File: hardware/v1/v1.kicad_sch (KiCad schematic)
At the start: 70 parts, among them J1 AUDIO IN, J10 Close for battery power, J2 MIDI OUT, J3 MIDI IN, J4 MIDI THRU, J5 OUTPUT R, J6 OUTPUT L - MONO, J7 EXP 2, J8 EXP 1, J9 Batt In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

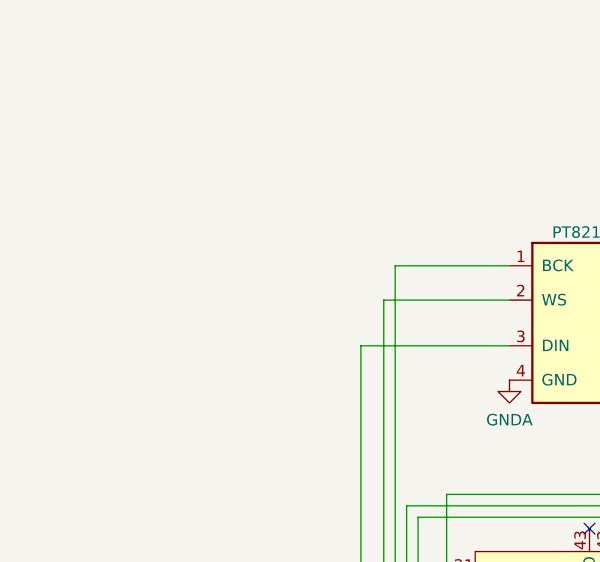
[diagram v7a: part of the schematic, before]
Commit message: Added mounting holes - Cleaned PCB placement
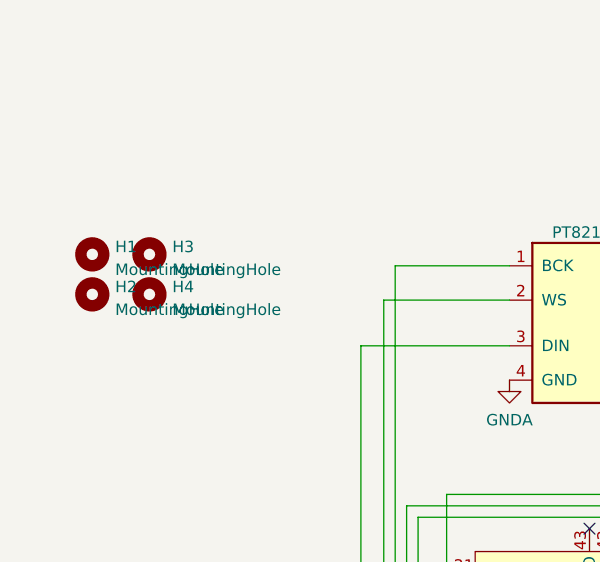
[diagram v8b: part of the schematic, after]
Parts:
- added H1, H2, H3, H4: MountingHole, MountingHole:MountingHole_3.2mm_M3_ISO14580, symbol Mechanical:MountingHole
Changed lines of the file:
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@@
     (pin "8")
+  )
+  (symbol (lib_id "Mechanical:MountingHole") (at 26.035 31.75 0) (unit 1)
+    (in_bom yes) (on_board yes) (fields_autoplaced)
+    (property "Reference" "H1" (id 0) (at 28.575 30.9153 0)
+      (effects (font (size 1.27 1.27)) (justify left))
+    )
+    (property "Value" "MountingHole" (id 1) (at 28.575 33.4522 0)
+      (effects (font (size 1.27 1.27)) (justify left))
+    )
+    (property "Footprint" "MountingHole:MountingHole_3.2mm_M3_ISO14580" (id 2) (at 26.035 31.75 0)
+      (effects (font (size 1.27 1.27)) hide)
+    )
+    (property "Datasheet" "~" (id 3) (at 26.035 31.75 0)
+      (effects (font (size 1.27 1.27)) hide)
+    )
   )
   (symbol (lib_id "power:+3V3") (at 159.385 73.66 90) (unit 1)
@@
     (pin "4")
   )
+  (symbol (lib_id "Mechanical:MountingHole") (at 32.385 31.75 0) (unit 1)
+    (in_bom yes) (on_board yes) (fields_autoplaced)
+    (property "Reference" "H3" (id 0) (at 34.925 30.9153 0)
+      (effects (font (size 1.27 1.27)) (justify left))
+    )
+    (property "Value" "MountingHole" (id 1) (at 34.925 33.4522 0)
+      (effects (font (size 1.27 1.27)) (justify left))
+    )
+    (property "Footprint" "MountingHole:MountingHole_3.2mm_M3_ISO14580" (id 2) (at 32.385 31.75 0)
+      (effects (font (size 1.27 1.27)) hide)
+    )
+    (property "Datasheet" "~" (id 3) (at 32.385 31.75 0)
+      (effects (font (size 1.27 1.27)) hide)
+    )
+  )
   (symbol (lib_id "Device:C_Polarized") (at 455.295 149.225 180) (unit 1)
     (in_bom yes) (on_board yes) (fields_autoplaced)
@@
     (pin "4")
   )
+  (symbol (lib_id "Mechanical:MountingHole") (at 26.035 36.195 0) (unit 1)
+    (in_bom yes) (on_board yes) (fields_autoplaced)
+    (property "Reference" "H2" (id 0) (at 28.575 35.3603 0)
+      (effects (font (size 1.27 1.27)) (justify left))
+    )
+    (property "Value" "MountingHole" (id 1) (at 28.575 37.8972 0)
+      (effects (font (size 1.27 1.27)) (justify left))
+    )
+    (property "Footprint" "MountingHole:MountingHole_3.2mm_M3_ISO14580" (id 2) (at 26.035 36.195 0)
+      (effects (font (size 1.27 1.27)) hide)
+    )
+    (property "Datasheet" "~" (id 3) (at 26.035 36.195 0)
+      (effects (font (size 1.27 1.27)) hide)
+    )
+  )
   (symbol (lib_id "Amplifier_Operational:TL074") (at 408.94 120.015 0) (unit 2)
     (in_bom yes) (on_board yes) (fields_autoplaced)
@@
     (pin "2")
     (pin "3")
+  )
+  (symbol (lib_id "Mechanical:MountingHole") (at 32.385 36.195 0) (unit 1)
+    (in_bom yes) (on_board yes) (fields_autoplaced)
+    (property "Reference" "H4" (id 0) (at 34.925 35.3603 0)
+      (effects (font (size 1.27 1.27)) (justify left))
+    )
+    (property "Value" "MountingHole" (id 1) (at 34.925 37.8972 0)
+      (effects (font (size 1.27 1.27)) (justify left))
+    )
+    (property "Footprint" "MountingHole:MountingHole_3.2mm_M3_ISO14580" (id 2) (at 32.385 36.195 0)
+      (effects (font (size 1.27 1.27)) hide)
+    )
+    (property "Datasheet" "~" (id 3) (at 32.385 36.195 0)
+      (effects (font (size 1.27 1.27)) hide)
+    )
   )
   (symbol (lib_id "power:+3.3V") (at 191.135 137.795 90) (unit 1)
@@
       (reference "D1") (unit 1) (value "1N914") (footprint "Diode_THT:D_DO-34_SOD68_P7.62mm_Horizontal")
     )
+    (path "/1b38fedc-9922-4b9f-a208-ce686a48a281"
+      (reference "H1") (unit 1) (value "MountingHole") (footprint "MountingHole:MountingHole_3.2mm_M3_ISO14580")
+    )
+    (path "/716e12c1-8bb1-4d40-9e17-8109f40cc3b6"
+      (reference "H2") (unit 1) (value "MountingHole") (footprint "MountingHole:MountingHole_3.2mm_M3_ISO14580")
+    )
+    (path "/66c12bc5-3179-47f4-bb5e-65b70f04e9af"
+      (reference "H3") (unit 1) (value "MountingHole") (footprint "MountingHole:MountingHole_3.2mm_M3_ISO14580")
+    )
+    (path "/82c939ff-8f1e-46db-87e3-d96ec50f6e3c"
+      (reference "H4") (unit 1) (value "MountingHole") (footprint "MountingHole:MountingHole_3.2mm_M3_ISO14580")
+    )
     (path "/6d8f37bb-f159-4e1e-a9e9-050f40456d61"
